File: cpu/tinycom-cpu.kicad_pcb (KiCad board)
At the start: 4 copper layers, 39.9 x 41.4 mm, 10 parts, among them P1 CONN_02X08, P2 CONN_02X08, U1 OLIMEX_IC_A13, U2 H5TQ2G83BFR/FBGA82, Y1 Crystal

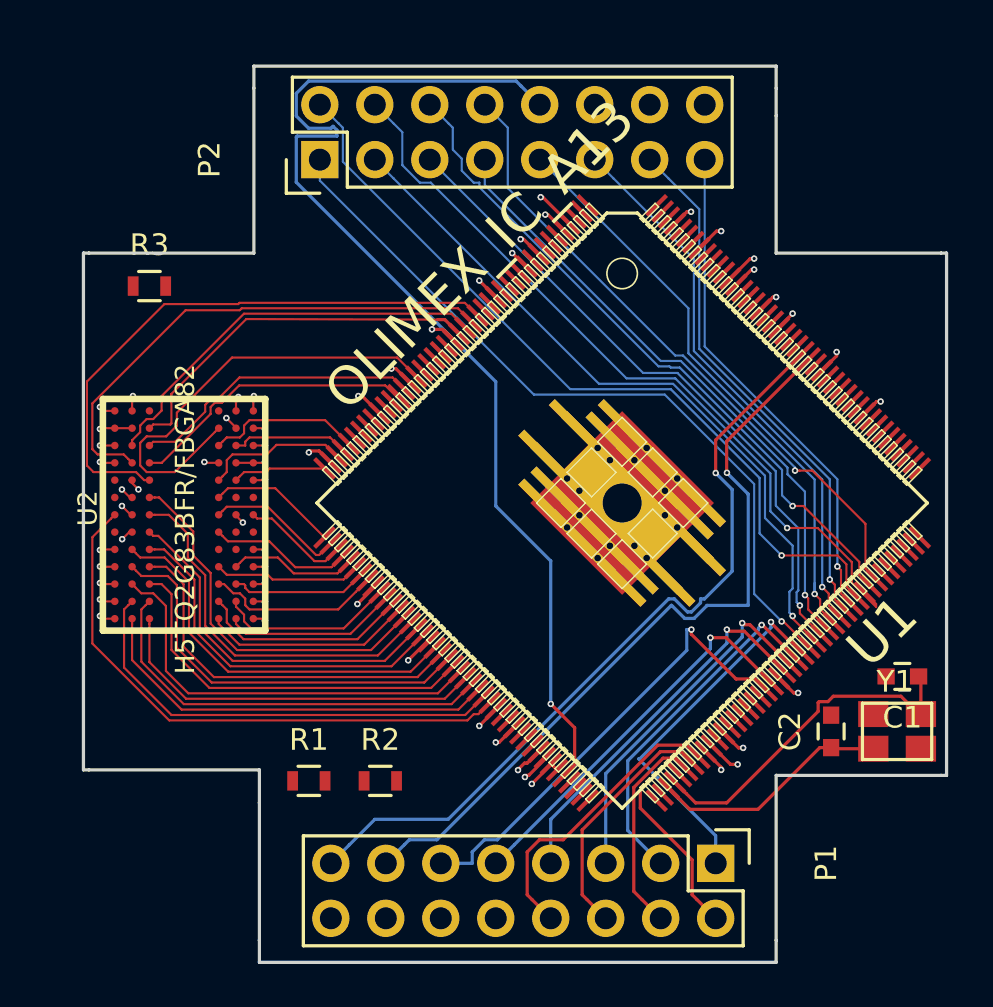
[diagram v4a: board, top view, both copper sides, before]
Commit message: add missing routes in ddr
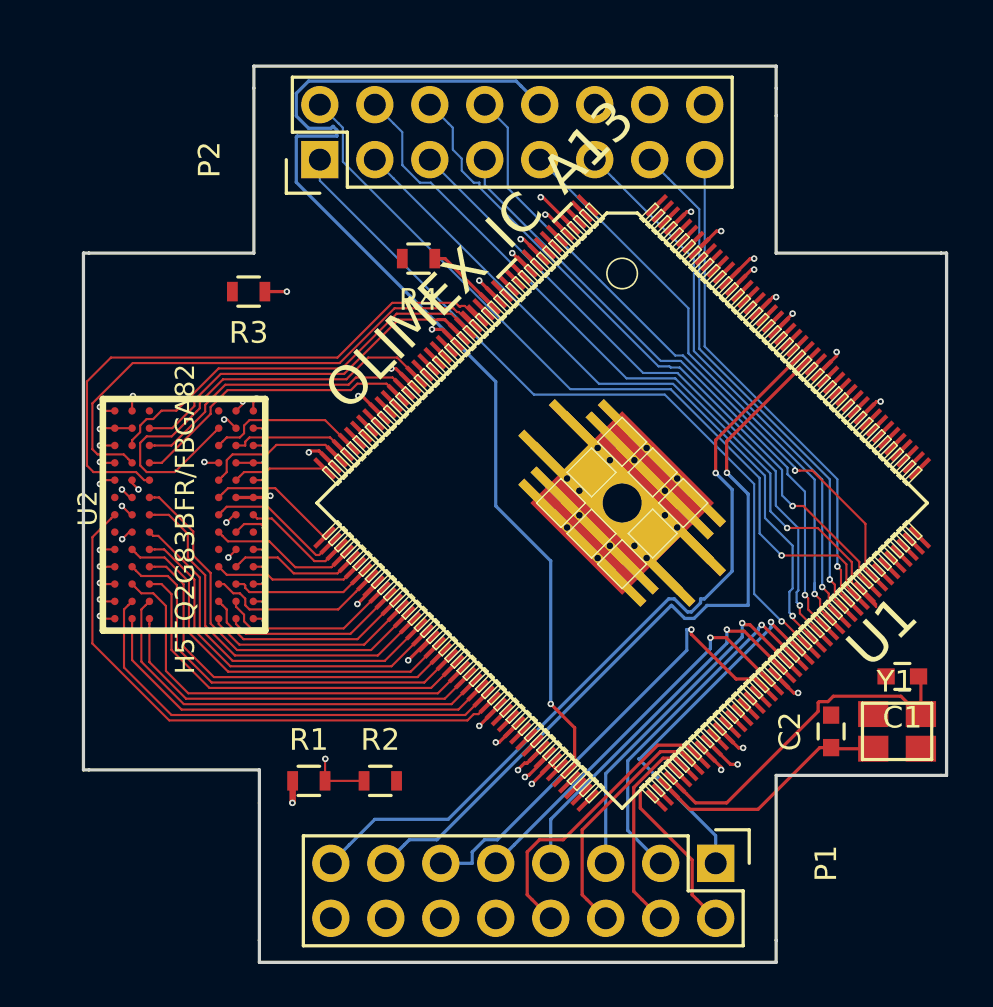
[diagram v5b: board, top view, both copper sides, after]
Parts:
- added R4: R, Resistors_SMD:R_0603, F.Cu at (94.0, 99.3)
- moved R3 4.59 mm to (86.1, 100.8), turned to 180 degrees
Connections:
- U1 pad 157: Net-(U1-Pad157) -> GND
- U1 pad 18: Net-(U1-Pad18) -> GND
- U2 pad F9: Net-(U2-PadF9) -> GND
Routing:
- net Net-(R1-Pad2): track 0.00 -> 23.9 mm, vias 0 -> 3
- net Net-(R3-Pad1): track 0.00 -> 13.9 mm, vias 0 -> 2
- net VCC_15: track 84.3 -> 76.9 mm, vias 18 -> 19
- net Net-(R4-Pad1): track 0.00 -> 3.40 mm
- net DDR3_DQS0_N: track 15.0 -> 13.4 mm
- net GND: track 12.2 -> 13.7 mm, vias 16 -> 17
- net DDR3_D0: track 17.5 -> 16.8 mm
- removed copper zone on In2.Cu, net VCC_15
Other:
- net class Default: trace_width 0.15 -> 0.1

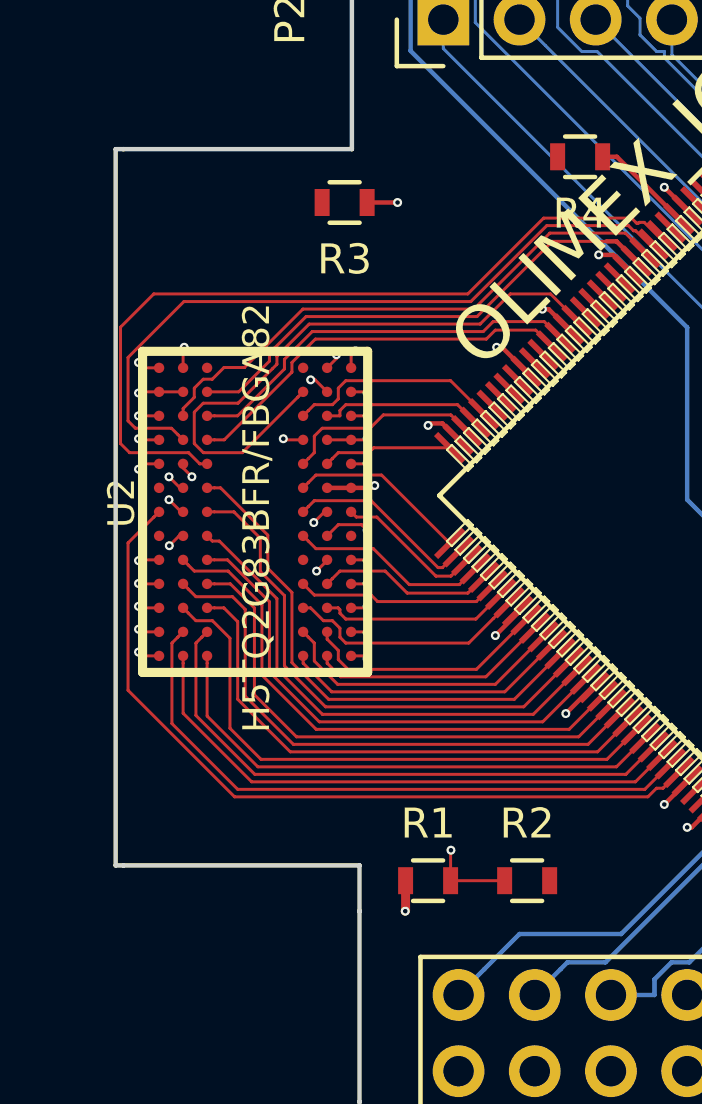
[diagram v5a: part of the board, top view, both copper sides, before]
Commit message: add some capacitors
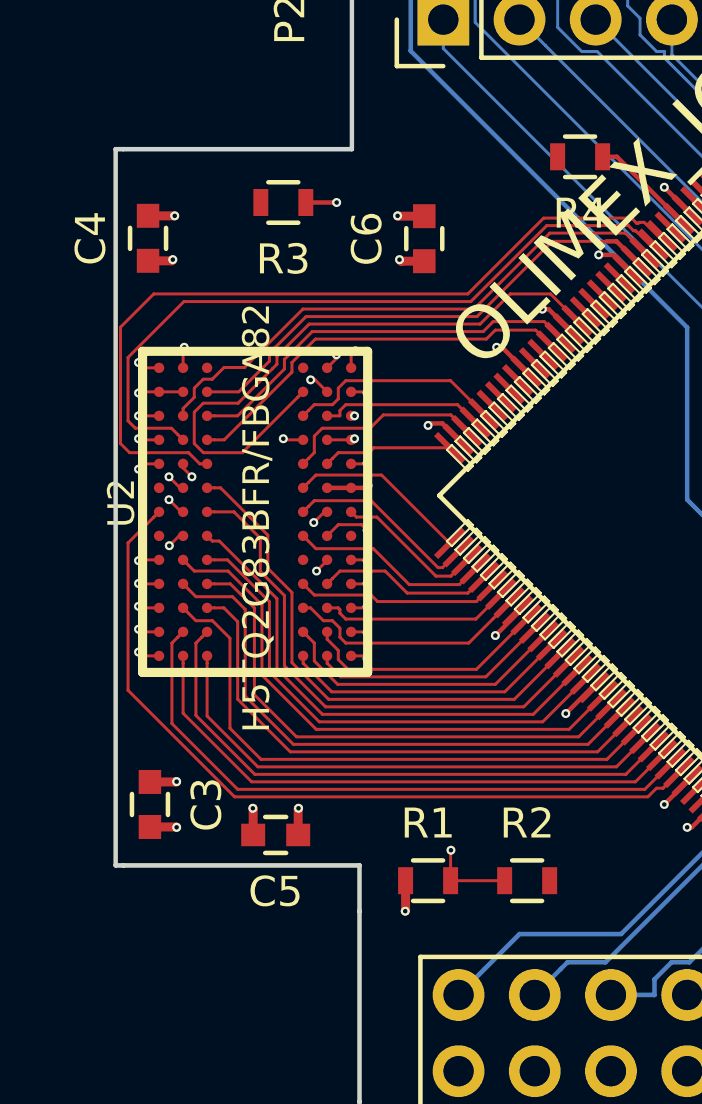
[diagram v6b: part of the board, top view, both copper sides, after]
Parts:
- added C3: 100nF, Capacitors_SMD:C_0603, F.Cu at (79.6, 120.9)
- added C4: 100nF, Capacitors_SMD:C_0603, F.Cu at (79.6, 102.0)
- added C5: 100nF, Capacitors_SMD:C_0603, F.Cu at (83.8, 121.9)
- added C6: 100nF, Capacitors_SMD:C_0603, F.Cu at (88.8, 102.0)
- C1, C2: value C_Small -> 33pF
- R1, R2: value R -> 1K
- R3, R4: value R -> 240R
- moved R3 2.04 mm to (84.1, 100.8)
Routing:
- net VCC_15: track 76.9 -> 90.7 mm, vias 19 -> 23
- net GND: track 13.7 -> 16.2 mm, vias 17 -> 21
- net (no net): track 0.00 -> 0.52 mm
- added copper zone on In2.Cu, net VCC_15

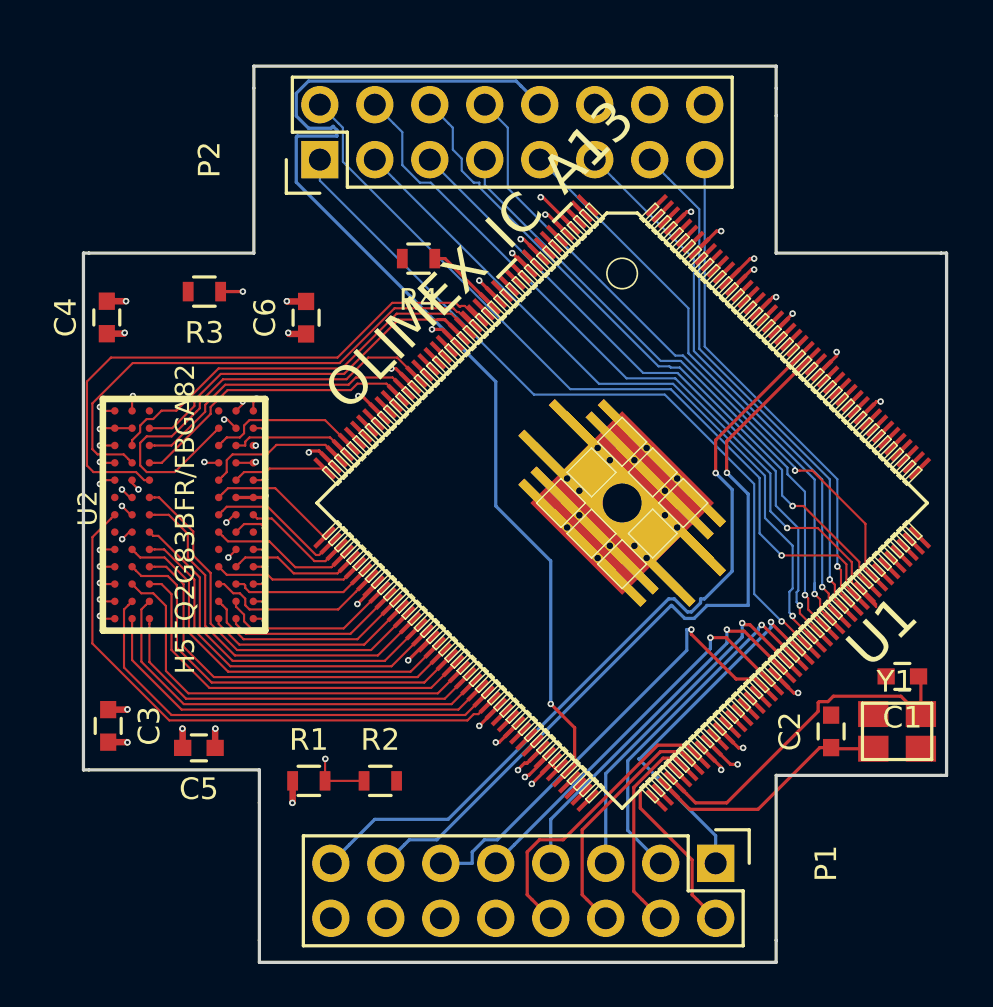
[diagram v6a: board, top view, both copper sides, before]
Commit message: add more capacitors
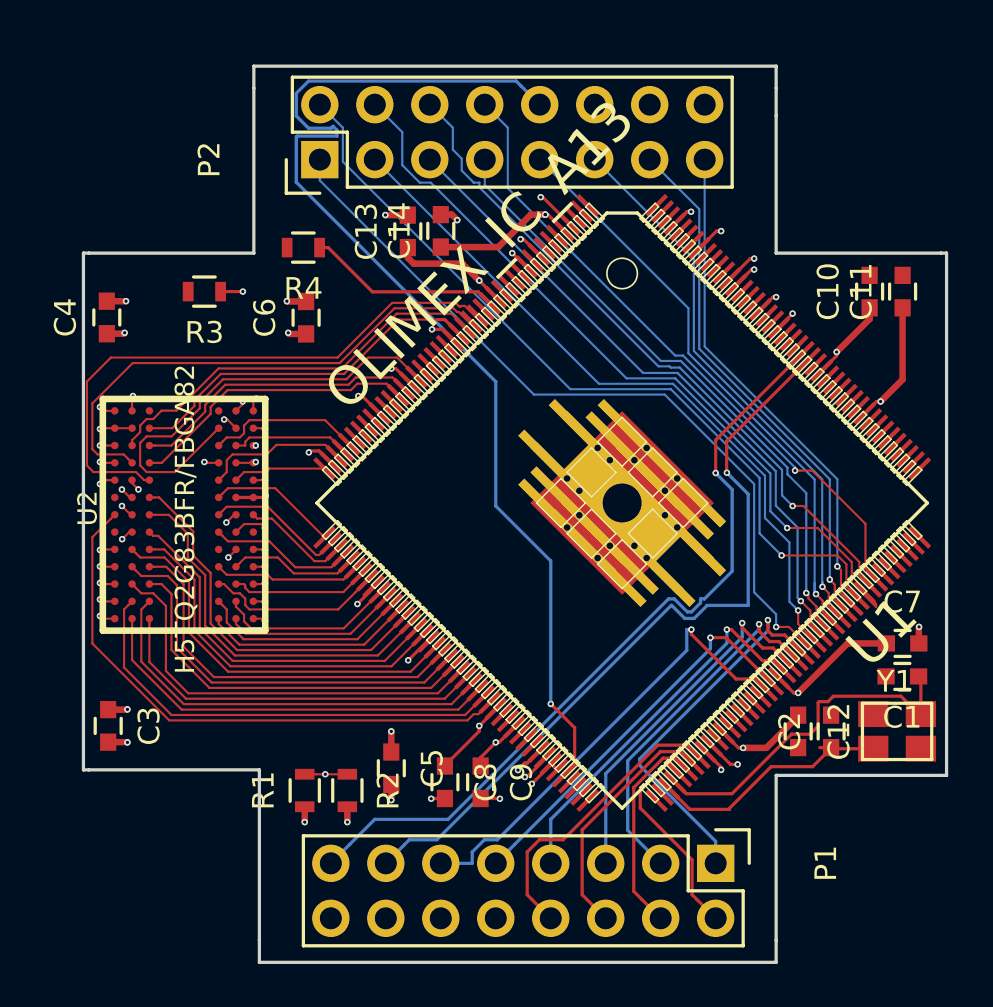
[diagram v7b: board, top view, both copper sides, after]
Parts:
- added C10: 100nF, Capacitors_SMD:C_0603, F.Cu at (114.8, 100.8)
- added C11: 100nF, Capacitors_SMD:C_0603, F.Cu at (116.3, 100.8)
- added C12: 100nF, Capacitors_SMD:C_0603, F.Cu at (111.5, 121.2)
- added C13: 100nF, Capacitors_SMD:C_0603, F.Cu at (93.5, 98.1)
- added C14: 100nF, Capacitors_SMD:C_0603, F.Cu at (95.0, 98.0)
- added C7: 100nF, Capacitors_SMD:C_0603, F.Cu at (116.3, 117.1)
- added C8: 100nF, Capacitors_SMD:C_0603, F.Cu at (95.2, 123.5)
- added C9: 100nF, Capacitors_SMD:C_0603, F.Cu at (96.8, 123.5)
- moved C5 8.94 mm to (92.7, 122.9), turned to 270 degrees
- moved R4 5.35 mm to (88.6, 98.8)
- moved R2 1.59 mm to (90.7, 123.9), turned to 270 degrees
- moved R1 0.48 mm to (88.7, 123.9), turned to 90 degrees
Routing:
- net VCC_33: track 83.1 -> 97.8 mm, vias 8 -> 9
- net VCC_14: track 112.2 -> 126.6 mm
- net VCC_15: track 90.7 -> 81.4 mm
- net Net-(R4-Pad1): track 3.40 -> 8.93 mm
- net GND: track 16.2 -> 21.0 mm, vias 21 -> 27
- net Net-(C2-Pad1): track 11.0 -> 11.6 mm
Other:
- net class Default: trace_width 0.1 -> 0.15

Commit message: change to 0805 components
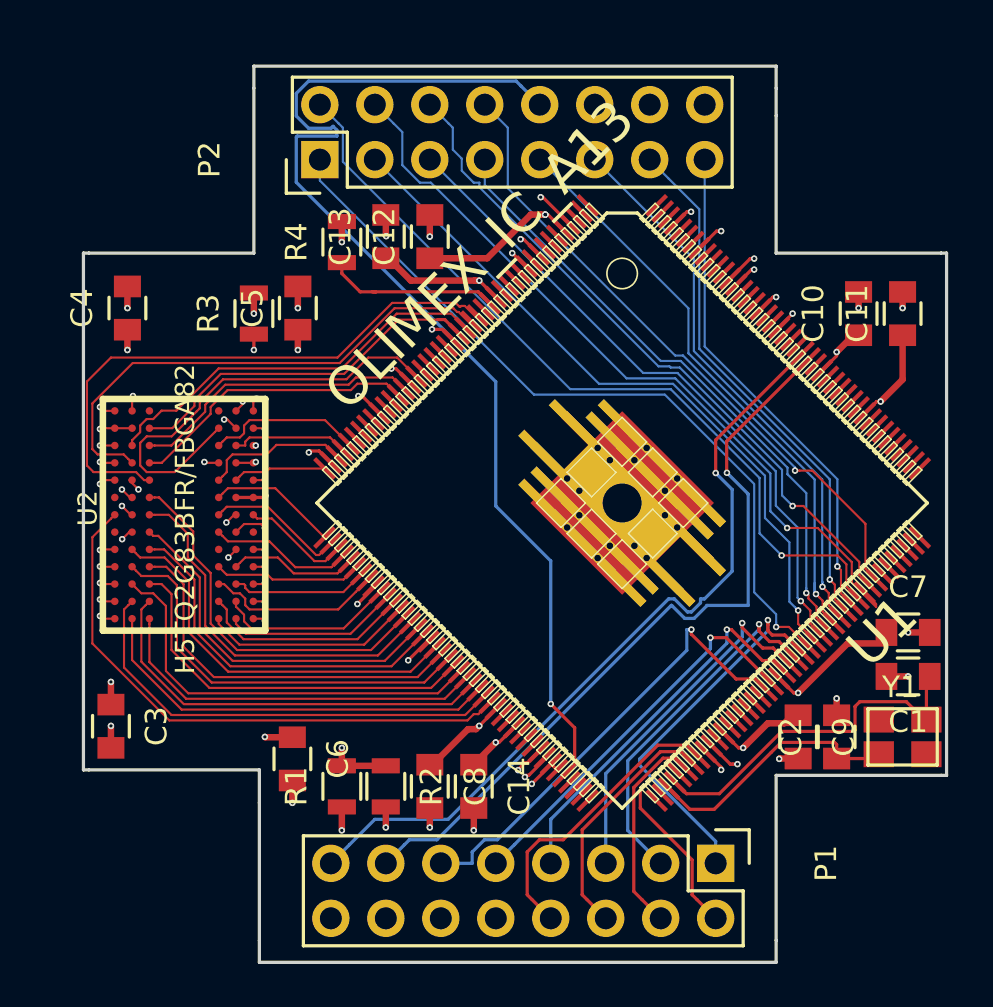
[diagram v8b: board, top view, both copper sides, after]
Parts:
- C1, C10, C11, C12, C13, C14, C2, C3, C4, C5, C6, C7, C8, C9: footprint Capacitors_SMD:C_0603 -> Capacitors_SMD:C_0805
- R1, R2, R3, R4: footprint Resistors_SMD:R_0603 -> Resistors_SMD:R_0805
- moved C12 28.5 mm to (94.5, 98.3), turned to 90 degrees
- moved C14 25.7 mm to (96.5, 123.7), turned to 270 degrees
- moved C5 21.7 mm to (88.4, 101.6), turned to 90 degrees
- moved C6 20.4 mm to (88.1, 122.4), turned to 270 degrees
- moved C9 14.8 mm to (111.5, 121.4)
- moved R3 2.50 mm to (86.4, 101.9), turned to 90 degrees
- moved R4 1.80 mm to (90.4, 98.6), turned to 90 degrees
- moved R2 1.79 mm to (92.5, 123.7)
- moved R1 1.73 mm to (90.4, 123.7)
- moved C10 1.14 mm to (114.3, 101.9)
- moved C4 1.05 mm to (80.5, 101.6)
- moved C13 1.04 mm to (92.5, 98.3)
- moved C11 1.02 mm to (116.3, 101.9)
- moved C8 0.72 mm to (94.5, 123.7)
- moved C7 0.57 mm to (116.6, 116.6)
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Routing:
- net VCC_15: track 81.4 -> 70.0 mm
- net GND: track 21.0 -> 28.6 mm, vias 27 -> 34
- net Net-(R3-Pad1): track 14.2 -> 11.2 mm
- net Net-(R1-Pad2): track 23.7 -> 25.6 mm
- net Net-(R4-Pad1): track 8.93 -> 8.06 mm
- net Net-(C2-Pad1): track 11.6 -> 12.2 mm
- net Net-(C1-Pad1): track 16.2 -> 16.7 mm
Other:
- board text added: "TinyCom"
- board text added: "http://tinycom.org/"
